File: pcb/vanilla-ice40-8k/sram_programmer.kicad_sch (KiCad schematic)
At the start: 32 parts, among them U2 W25X40CLSN, U3 FT2232HQ, U4 93LCxxBxxOT, Y1 12Mhz/18pf

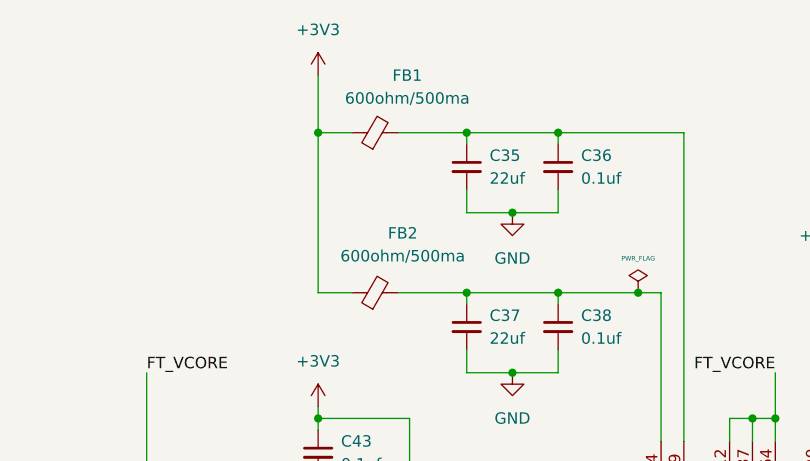
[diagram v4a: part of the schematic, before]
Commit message: [hx8k][pcb] move programmer to symbol lib
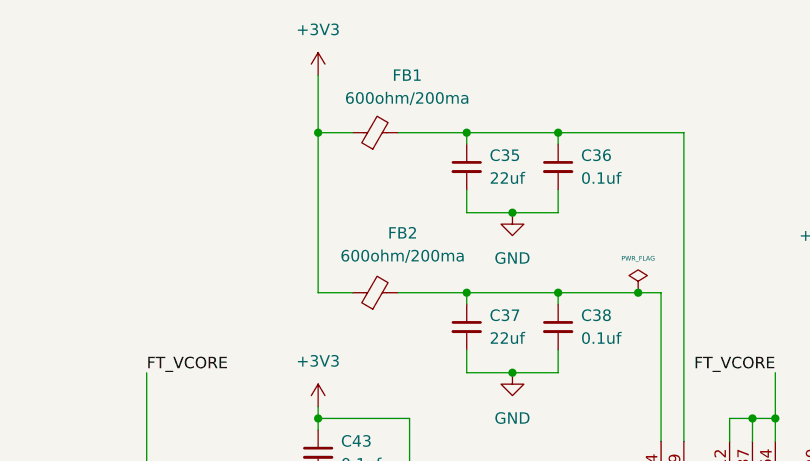
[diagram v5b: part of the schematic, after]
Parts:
- removed U4: 93LCxxBxxOT, Package_TO_SOT_SMD:SOT-23-6, symbol Memory_EEPROM:93LCxxBxxOT
- added U4: 93LCxxBxxOT, Package_TO_SOT_SMD:SOT-23-6, symbol !Misc:93LCxxBxxOT
- C49, C50: symbol Device:C_Small -> !Misc:C_27pf_0402
- FB1, FB2: value 600ohm/500ma -> 600ohm/200ma; symbol Device:FerriteBead_Small -> !Misc:FB_600; Digi-Key Part Number 490-5258-1-ND -> 240-2399-1-ND; LCSC Part # C1002 -> C1017
- U2: symbol Memory_Flash:W25X40CLSN -> !Misc:W25X40CLSN
- Y1: symbol Device:Crystal_GND24_Small -> !Misc:Crystal_12MHz; Digi-Key Part Number 535-10261-1-ND -> 535-14963-1-ND; LCSC Part # C390764 -> C9002
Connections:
- net +3V3: now also U4.6 (VCC)
- net GND: now also U4.2 (GND)
- net at R26.2, R29.1: now also U4.1 (DO)
- net at R29.2, U3.61 (EEDATA): now also U4.3 (DI)
- net at R27.2, U3.62 (EECLK): now also U4.4 (CLK)
- net at R28.2, U3.63 (EECS): now also U4.5 (CS)
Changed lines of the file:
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@@
 	)
 	(symbol
-		(lib_id "Device:C_Small")
+		(lib_id "!Misc:C_27pf_0402")
 		(at 90.17 180.34 270)
 		(unit 1)
@@
 			)
 		)
-		(property "Description" "Unpolarized capacitor, small symbol"
+		(property "Description" "Unpolarized capacitor 33pf 0402"
 			(at 90.17 180.34 0)
 			(effects
@@
 	)
 	(symbol
-		(lib_id "Memory_Flash:W25X40CLSN")
+		(lib_id "!Misc:W25X40CLSN")
 		(at 266.7 133.35 0)
 		(unit 1)
@@
 	)
 	(symbol
-		(lib_id "Device:C_Small")
+		(lib_id "!Misc:C_27pf_0402")
 		(at 90.17 190.5 270)
 		(unit 1)
@@
 			)
 		)
-		(property "Description" "Unpolarized capacitor, small symbol"
+		(property "Description" "Unpolarized capacitor 33pf 0402"
 			(at 90.17 190.5 0)
 			(effects
@@
 	)
 	(symbol
-		(lib_id "Device:FerriteBead_Small")
+		(lib_id "!Misc:FB_600")
 		(at 100.33 59.69 90)
 		(unit 1)
@@
 			)
 		)
-		(property "Value" "600ohm/500ma"
+		(property "Value" "600ohm/200ma"
 			(at 103.886 55.88 90)
 			(effects
@@
 			)
 		)
-		(property "Description" "Ferrite bead, small symbol"
+		(property "Description" "Ferrite bead, 600ohm, 0603, 200ma"
 			(at 100.33 59.69 0)
 			(effects
@@
 			)
 		)
-		(property "LCSC Part #" "C1002"
+		(property "LCSC Part #" "C1017"
 			(at 100.33 59.69 0)
 			(effects
@@
 			)
 		)
-		(property "Digi-Key Part Number" "490-5258-1-ND "
+		(property "Digi-Key Part Number" "240-2399-1-ND"
 			(at 100.33 59.69 0)
 			(effects
@@
 	)
 	(symbol
+		(lib_id "!Misc:93LCxxBxxOT")
+		(at 53.34 172.72 0)
+		(unit 1)
+		(exclude_from_sim no)
+		(in_bom yes)
+		(on_board yes)
+		(dnp no)
+		(property "Reference" "U4"
+			(at 35.306 180.086 0)
+			(effects
+				(font
+					(size 1.27 1.27)
+				)
+				(justify left)
+			)
+		)
+		(property "Value" "93LCxxBxxOT"
+			(at 35.306 182.626 0)
+			(effects
+				(font
+					(size 1.27 1.27)
+				)
+				(justify left)
+			)
+		)
+		(property "Footprint" "Package_TO_SOT_SMD:SOT-23-6"
+			(at 53.34 172.72 0)
+			(effects
+				(font
+					(size 1.27 1.27)
+				)
+				(hide yes)
+			)
+		)
+		(property "Datasheet" "http://ww1.microchip.com/downloads/en/DeviceDoc/20001749K.pdf"
+			(at 53.34 172.72 0)
+			(effects
+				(font
+					(size 1.27 1.27)
+				)
+				(hide yes)
+			)
+		)
+		(property "Description" "Serial EEPROM, 93 Series, 2.5V, SOT-23-6"
+			(at 53.34 172.72 0)
+			(effects
+				(font
+					(size 1.27 1.27)
+				)
+				(hide yes)
+			)
+		)
+		(property "LCSC Part #" "C190271"
+			(at 53.34 172.72 0)
+			(effects
+				(font
+					(size 1.27 1.27)
+				)
+				(hide yes)
+			)
+		)
+		(property "JLCPCB Rotation Offset" ""
+			(at 53.34 172.72 0)
+			(effects
+				(font
+					(size 1.27 1.27)
+				)
+				(hide yes)
+			)
+		)
+		(property "Digi-Key Part Number" "93LC56BT-I/OTCT-ND"
+			(at 53.34 172.72 0)
+			(effects
+				(font
+					(size 1.27 1.27)
+				)
+				(hide yes)
+			)
+		)
+		(pin "2"
+		)
+		(pin "1"
+		)
+		(pin "5"
+		)
+		(pin "6"
+		)
+		(pin "4"
+		)
+		(pin "3"
+		)
+		(instances
+			(project "vanilla-ice40-8k"
+				(path "/6fdfbf4b-014a-4077-8dc3-7ce5ecaf5fe5/8fcffd86-9b82-4947-9420-a56f34009c5e"
+					(reference "U4")
+					(unit 1)
+				)
+			)
+		)
+	)
+	(symbol
 		(lib_id "power:GND")
 		(at 93.98 97.79 0)
@@
 	)
 	(symbol
-		(lib_id "Device:FerriteBead_Small")
+		(lib_id "!Misc:FB_600")
 		(at 100.33 77.47 90)
 		(unit 1)
@@
 			)
 		)
-		(property "Value" "600ohm/500ma"
+		(property "Value" "600ohm/200ma"
 			(at 103.378 73.406 90)
 			(effects
@@
 			)
 		)
-		(property "Description" "Ferrite bead, small symbol"
+		(property "Description" "Ferrite bead, 600ohm, 0603, 200ma"
 			(at 100.33 77.47 0)
 			(effects
@@
 			)
 		)
-		(property "LCSC Part #" "C1002"
+		(property "LCSC Part #" "C1017"
 			(at 100.33 77.47 0)
 			(effects
@@
 			)
 		)
-		(property "Digi-Key Part Number" "490-5258-1-ND "
+		(property "Digi-Key Part Number" "240-2399-1-ND"
 			(at 100.33 77.47 0)
 			(effects
@@
 	)
 	(symbol
-		(lib_id "Memory_EEPROM:93LCxxBxxOT")
-		(at 53.34 172.72 0)
-		(unit 1)
-		(exclude_from_sim no)
-		(in_bom yes)
-		(on_board yes)
-		(dnp no)
-		(property "Reference" "U4"
-			(at 35.306 180.086 0)
-			(effects
-				(font
-					(size 1.27 1.27)
-				)
-				(justify left)
-			)
-		)
-		(property "Value" "93LCxxBxxOT"
-			(at 35.306 182.626 0)
-			(effects
-				(font
-					(size 1.27 1.27)
-				)
-				(justify left)
-			)
-		)
-		(property "Footprint" "Package_TO_SOT_SMD:SOT-23-6"
-			(at 53.34 172.72 0)
-			(effects
-				(font
-					(size 1.27 1.27)
-				)
-				(hide yes)
-			)
-		)
-		(property "Datasheet" "http://ww1.microchip.com/downloads/en/DeviceDoc/20001749K.pdf"
-			(at 53.34 172.72 0)
-			(effects
-				(font
-					(size 1.27 1.27)
-				)
-				(hide yes)
-			)
-		)
-		(property "Description" "Serial EEPROM, 93 Series, 2.5V, SOT-23-6"
-			(at 53.34 172.72 0)
-			(effects
-				(font
-					(size 1.27 1.27)
-				)
-				(hide yes)
-			)
-		)
-		(property "LCSC Part #" "C190271"
-			(at 53.34 172.72 0)
-			(effects
-				(font
-					(size 1.27 1.27)
-				)
-				(hide yes)
-			)
-		)
-		(property "JLCPCB Rotation Offset" ""
-			(at 53.34 172.72 0)
-			(effects
-				(font
-					(size 1.27 1.27)
-				)
-				(hide yes)
-			)
-		)
-		(property "Digi-Key Part Number" "93LC56BT-I/OTCT-ND"
-			(at 53.34 172.72 0)
-			(effects
-				(font
-					(size 1.27 1.27)
-				)
-				(hide yes)
-			)
-		)
-		(property "MPN" ""
-			(at 53.34 172.72 0)
-			(effects
-				(font
-					(size 1.27 1.27)
-				)
-			)
-		)
-		(property "Sim.Device" ""
-			(at 53.34 172.72 0)
-			(effects
-				(font
-					(size 1.27 1.27)
-				)
-			)
-		)
-		(property "Sim.Pins" ""
-			(at 53.34 172.72 0)
-			(effects
-				(font
-					(size 1.27 1.27)
-				)
-			)
-		)
-		(property "Sim.Type" ""
-			(at 53.34 172.72 0)
-			(effects
-				(font
-					(size 1.27 1.27)
-				)
-			)
-		)
-		(pin "2"
-		)
-		(pin "1"
-		)
-		(pin "5"
-		)
-		(pin "6"
-		)
-		(pin "4"
-		)
-		(pin "3"
-		)
-		(instances
-			(project "vanilla-ice40-8k"
-				(path "/6fdfbf4b-014a-4077-8dc3-7ce5ecaf5fe5/8fcffd86-9b82-4947-9420-a56f34009c5e"
-					(reference "U4")
-					(unit 1)
-				)
-			)
-		)
-	)
-	(symbol
 		(lib_id "!Misc:R_10K_0603")
 		(at 67.31 162.56 0)
@@
 	)
 	(symbol
-		(lib_id "Device:Crystal_GND24_Small")
+		(lib_id "!Misc:Crystal_12MHz")
 		(at 100.33 185.42 90)
 		(unit 1)
@@
 			)
 		)
-		(property "Description" "Four pin crystal, GND on pins 2 and 4, small symbol"
+		(property "Description" "12MHz SMD crystal oscillator 18pF ±10ppm SMD3225-4P  Crystals ROHS"
 			(at 100.33 185.42 0)
 			(effects
@@
 			)
 		)
-		(property "LCSC Part #" "C390764"
+		(property "LCSC Part #" "C9002"
 			(at 100.33 185.42 0)
 			(effects
@@
 			)
 		)
-		(property "Digi-Key Part Number" "535-10261-1-ND"
+		(property "Digi-Key Part Number" "535-14963-1-ND"
 			(at 100.33 185.42 0)
 			(effects

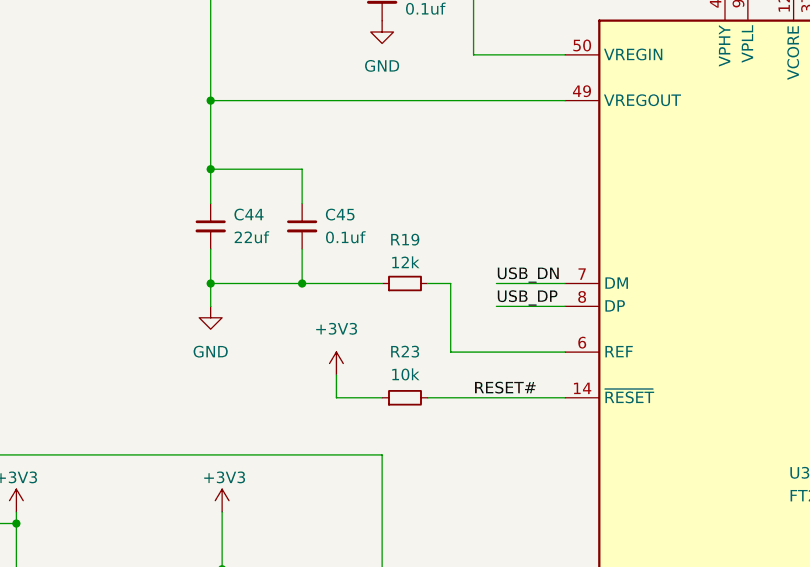
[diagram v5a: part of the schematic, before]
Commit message: [hx8k][pcb] start of routing of R signals below usb
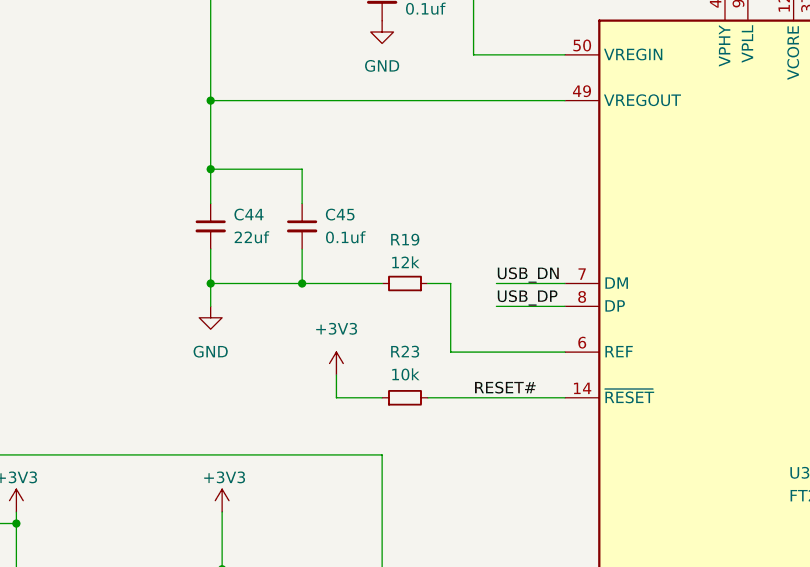
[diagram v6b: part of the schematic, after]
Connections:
- net GND: now also R19.2; no longer R19.1
- net at U3.6 (REF): now also R19.1; no longer R19.2
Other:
- moved on the sheet: R19
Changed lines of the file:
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@@
 		(on_board yes)
 		(dnp no)
-		(fields_autoplaced yes)
 		(property "Reference" "R23"
 			(at 96.52 134.62 90)
@@
 	(symbol
 		(lib_id "!Misc:R_2.2K_0603")
-		(at 96.52 127 90)
+		(at 96.52 127 270)
+		(mirror x)
 		(unit 1)
 		(exclude_from_sim no)

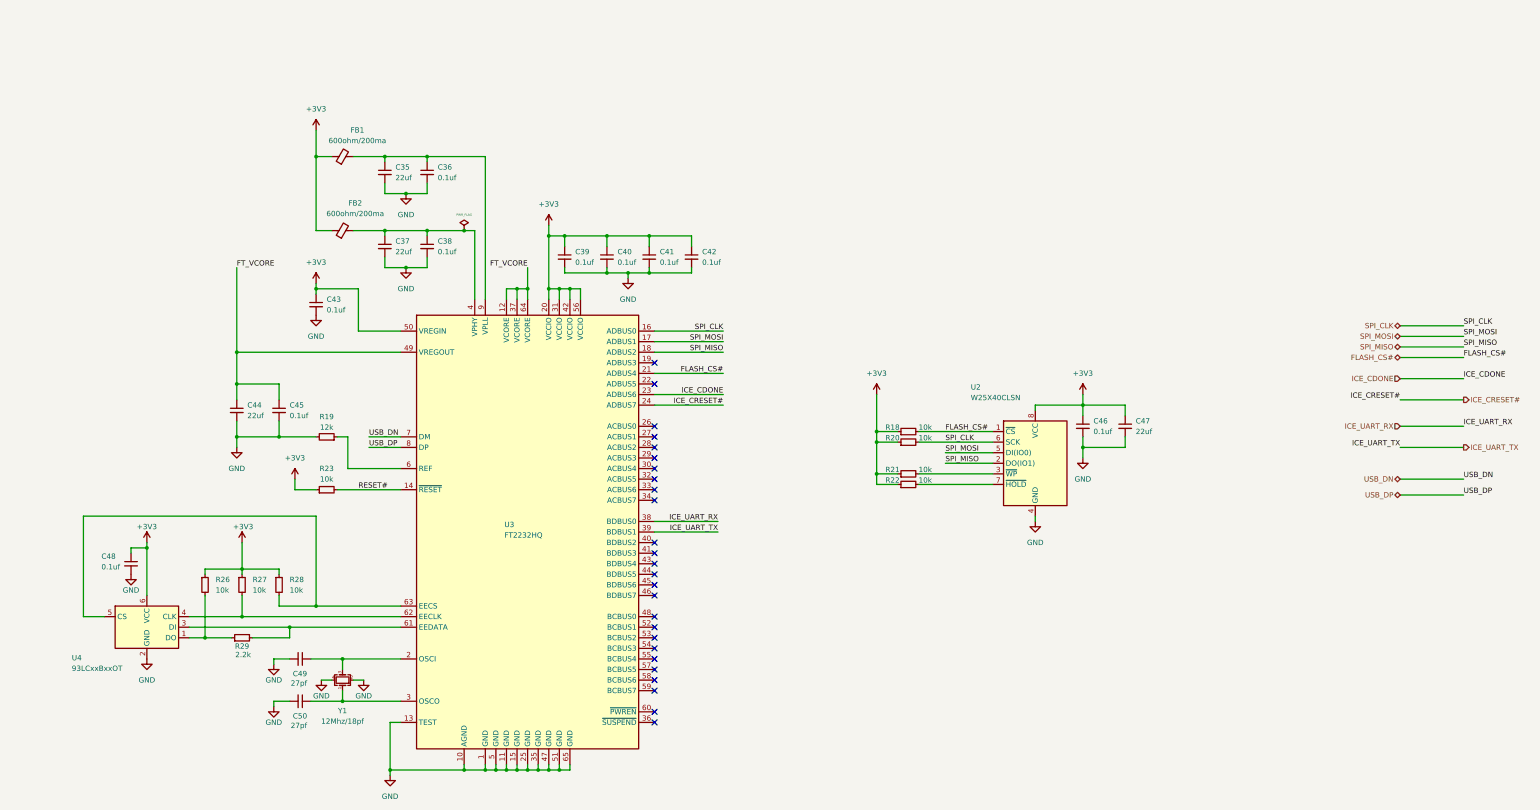
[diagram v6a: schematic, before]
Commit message: [hx8k][pcb] convert all components to custom lib
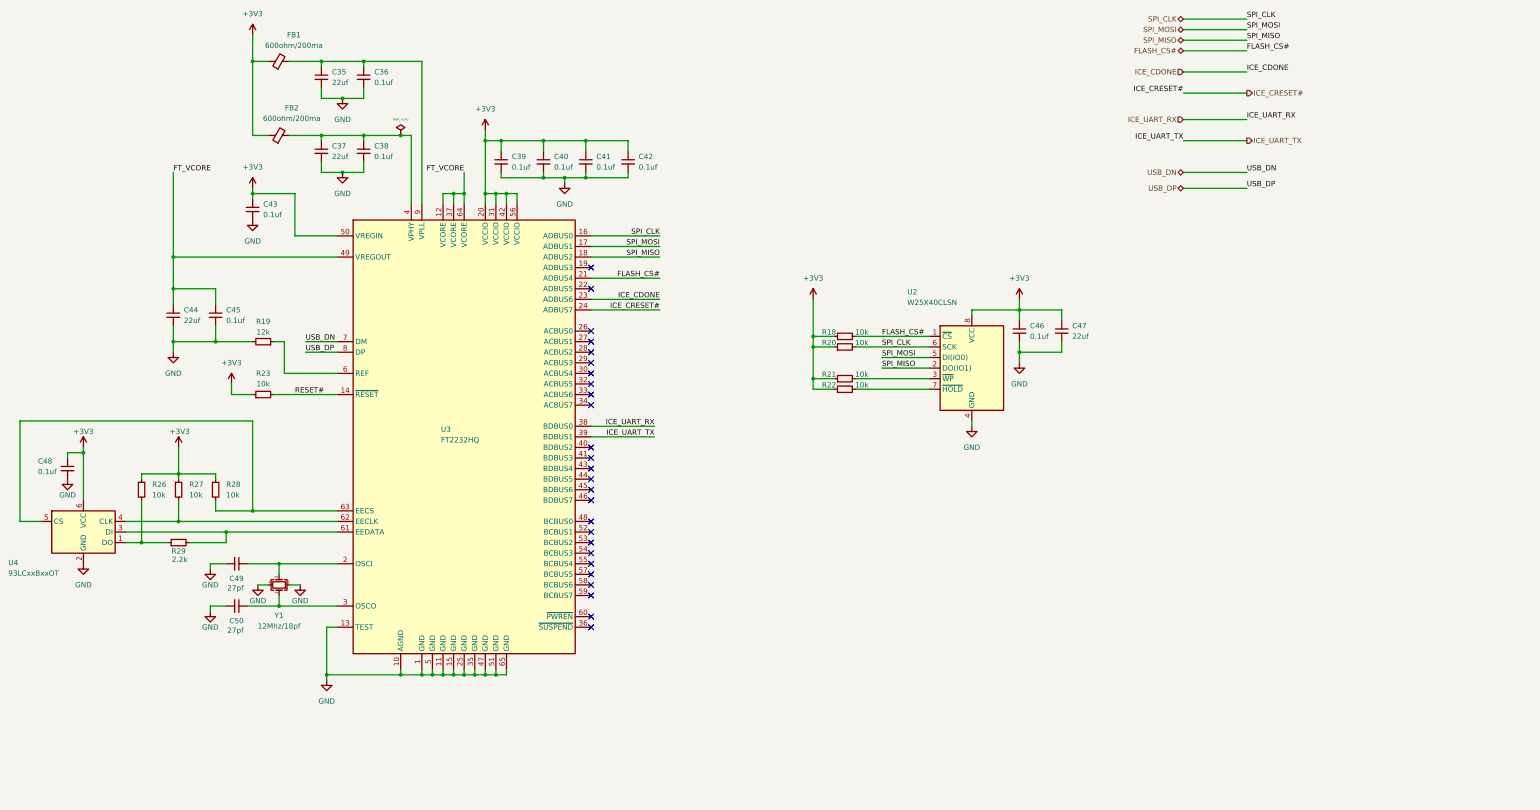
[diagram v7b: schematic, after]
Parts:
- R19: Digi-Key Part Number 118-CR0603-FX-1202ELFCT-ND -> 118-CR0603-FX-2201ELFCT-ND; LCSC Part # C22790 -> C25879
- R29: LCSC Part # C4190 -> C25879
- U3: JLCPCB Rotation Offset 90 -> (none)
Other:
- moved on the sheet: C35, C36, C37, C38, C39, C40, C41, C42, C43, C44, C45, C46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

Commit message: [pcb] misc fixes during jlcpcb production submission
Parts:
- FB1, FB2: Digi-Key Part Number 240-2399-1-ND -> 240-2371-1-ND; LCSC Part # C1017 -> C1002
- R19: symbol !Misc:R_2.2K_0603 -> !Misc:R_12K_0603; Digi-Key Part Number 118-CR0603-FX-2201ELFCT-ND -> 118-CR0603-FX-1202ELFCT-ND; LCSC Part # C25879 -> C22790
- R29: LCSC Part # C25879 -> C4190
